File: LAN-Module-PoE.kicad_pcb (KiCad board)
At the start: 2 copper layers, 25.3 x 61 mm, 135 parts, among them J1 HY931147C, J10 ProtoCastellatedHeader, J11 ProtoCastellatedHeader, J12 ProtoCastellatedHeader, J13 ProtoCastellatedHeader, J14 ProtoCastellatedHeader, J15 ProtoCastellatedHeader, J16 ProtoCastellatedHeader, J17 ProtoCastellatedHeader, J18 ProtoCastellatedHeader, J19 ProtoCastellatedHeader, J2 ProtoCastellatedHeader, J20 ProtoCastellatedHeader, J21 ProtoCastellatedHeader, J22 ProtoCastellatedHeader, J23 ProtoCastellatedHeader, J24 ProtoCastellatedHeader, J25 ProtoCastellatedHeader, J26 ProtoCastellatedHeader, J27 ProtoCastellatedHeader, J28 ProtoCastellatedHeader, J29 ProtoCastellatedHeader, J3 ProtoCastellatedHeader, J4 ProtoCastellatedHeader, J5 ProtoCastellatedHeader, J6 ProtoCastellatedHeader, J7 ProtoCastellatedHeader, J8 ProtoCastellatedHeader, J9 ProtoCastellatedHeader, SW1 RESET, U1 ESP32-U4WDH, U2 Si3404, U3 LV2842XLVDDCR, U4 RTL8201F, Y1 40MHz

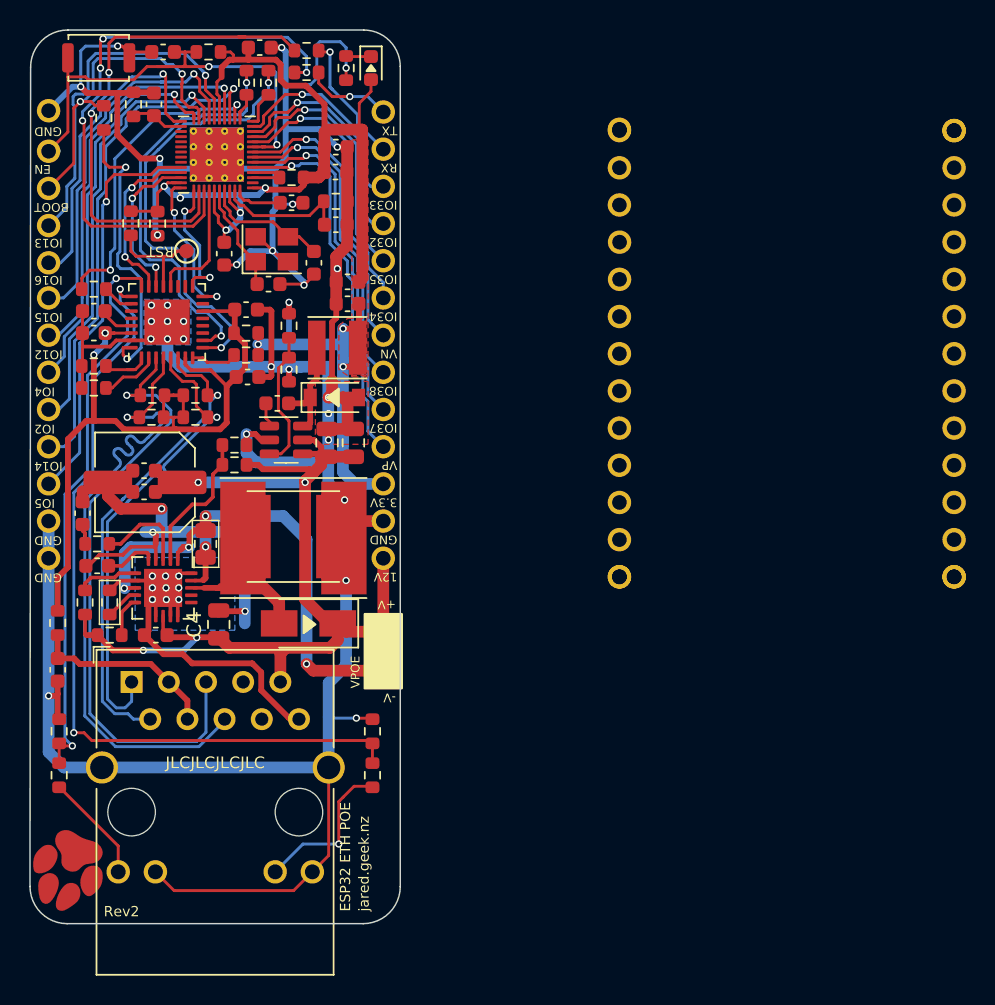
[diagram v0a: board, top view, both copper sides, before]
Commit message: HW REV: Fix stability issue
Important change required to ensure stability across different types of ethernet switches.

I had only tested this with a TP-LINK switch, but the design did not work with other switches, and the reference schematic does NOT specify that the CT/termination resistors should be tied to 3.3V. Instead they should be coupled to GND through a capacitor (of unspecified value).
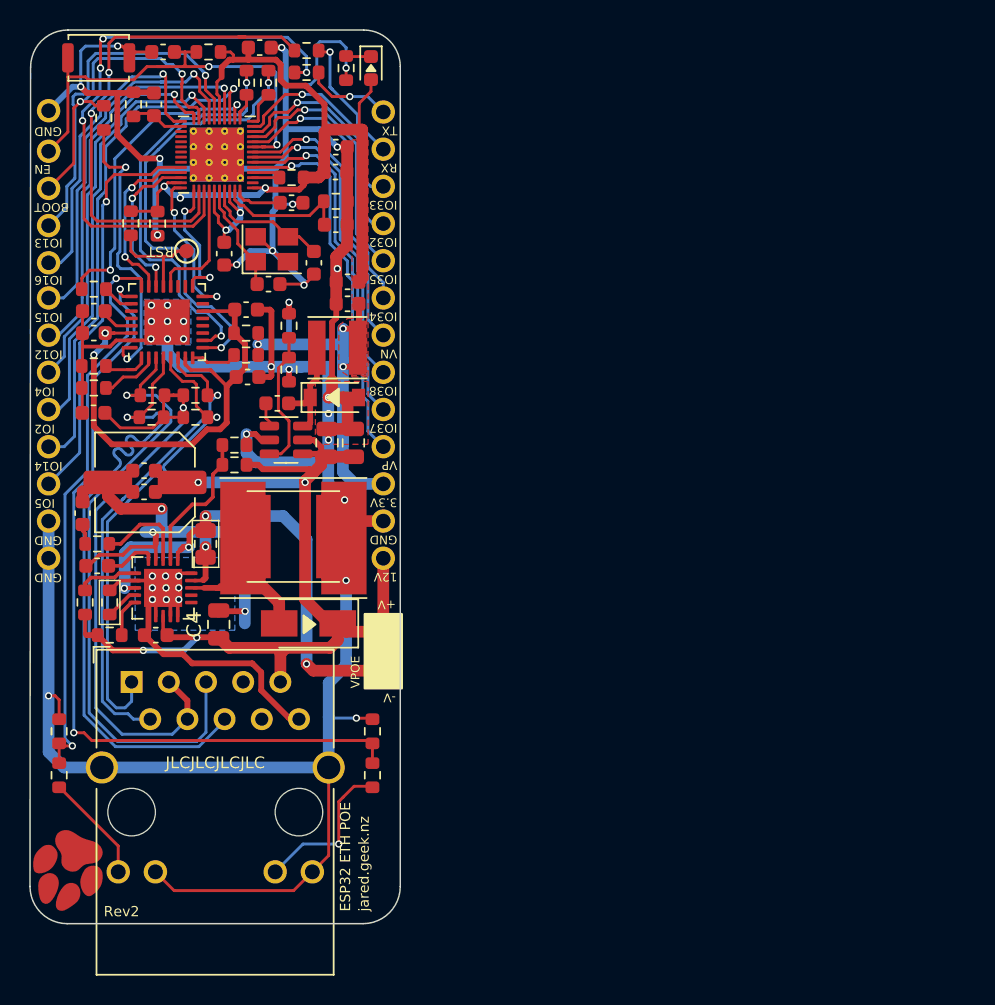
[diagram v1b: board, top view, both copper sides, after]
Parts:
- removed ? (x3): , 
- removed the J10 at (69.5, 57.1)
- removed the J11 at (69.5, 59.7)
- removed the J12 at (69.5, 62.2)
- removed the J13 at (69.5, 64.8)
- removed the J14 at (69.5, 67.3)
- removed the J15 at (92.3, 64.8)
- removed the J16 at (69.5, 69.8)
- removed the J17 at (92.3, 39.4)
- removed the J18 at (92.3, 41.9)
- removed the J19 at (92.3, 44.5)
- removed the J20 at (92.3, 47.0)
- removed the J21 at (92.3, 49.5)
- removed the J22 at (92.3, 52.1)
- removed the J23 at (92.3, 54.6)
- removed the J24 at (92.3, 57.1)
- removed the J25 at (92.3, 59.7)
- removed the J26 at (92.3, 62.2)
- removed the J27 at (92.3, 67.3)
- removed the J28 at (92.3, 69.8) (x2)
- removed the J3 at (69.5, 39.4)
- removed the J4 at (69.5, 41.9)
- removed the J5 at (69.5, 44.5)
- removed the J6 at (69.5, 47.0)
- removed the J7 at (69.5, 49.5)
- removed the J8 at (69.5, 52.1)
- removed the J9 at (69.5, 54.6)
- removed R25: 0R, Resistor_SMD:R_0603_1608Metric
- moved C3 17.7 mm to (33.5, 58.6), turned to 0 degrees
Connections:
- R13 pad 1: /LAN_3P3V -> /MDI0_CT
- R14 pad 1: /LAN_3P3V -> /MDI0_CT
- R17 pad 1: /LAN_3P3V -> /MDI0_CT
- R18 pad 1: /LAN_3P3V -> /MDI0_CT
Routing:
- net /MDI0_CT: track 12.9 -> 43.9 mm, vias 0 -> 1
- net /LAN_3P3V: track 53.6 -> 33.7 mm
- net GND: track 238.9 -> 236.3 mm
